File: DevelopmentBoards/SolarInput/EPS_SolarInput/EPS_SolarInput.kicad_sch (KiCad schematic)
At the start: 10 parts, among them J1 2053380004, J2 Conn_01x04_Socket, J3 Conn_01x02_Socket, J4 Conn_01x02_Pin, U1 INA232AIDDFR

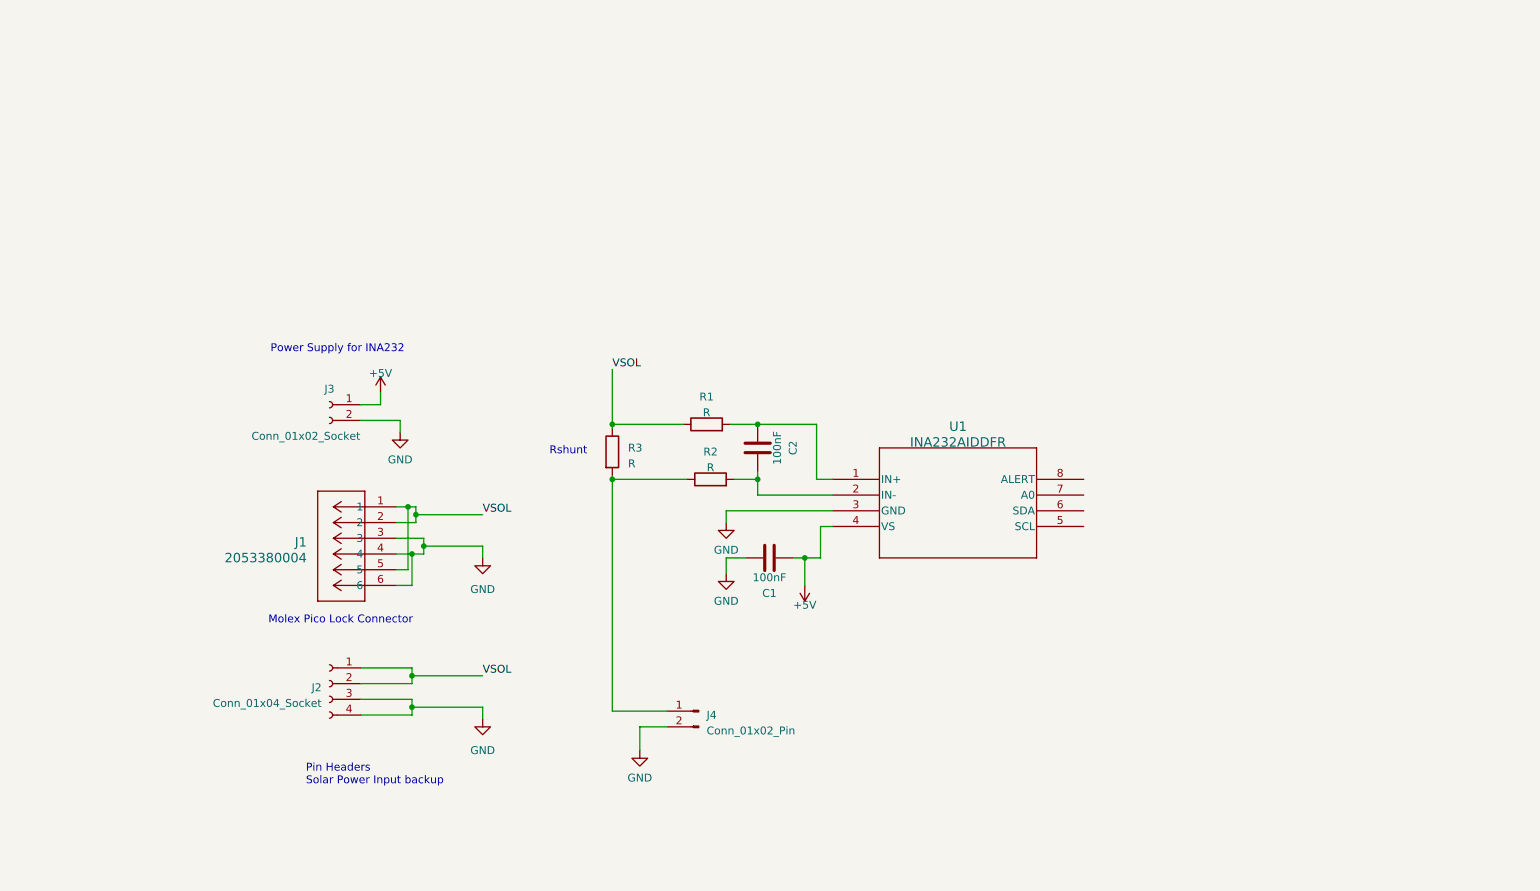
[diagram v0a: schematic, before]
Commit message: Completed EPS Solar Input Schematic
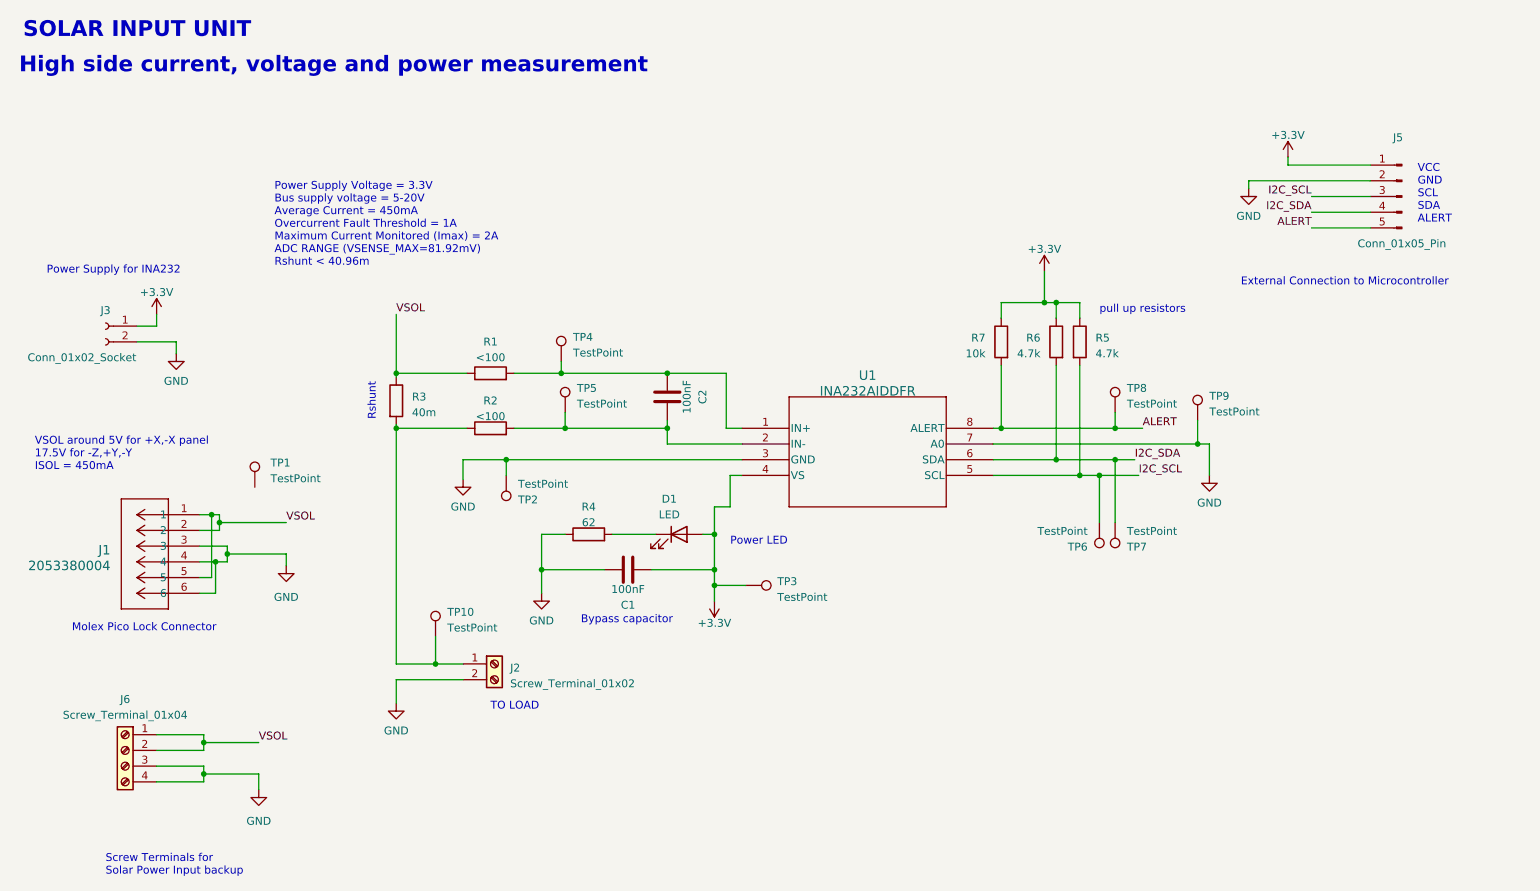
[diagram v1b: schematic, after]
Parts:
- removed J2: Conn_01x04_Socket, symbol Connector:Conn_01x04_Socket
- removed J4: Conn_01x02_Pin, symbol Connector:Conn_01x02_Pin
- added D1: LED, LED_SMD:LED_0805_2012Metric, symbol Device:LED
- added J2: Screw_Terminal_01x02, TerminalBlock_TE-Connectivity:TerminalBlock_TE_282834-2_1x02_P2.54mm_Horizontal, symbol Connector:Screw_Terminal_01x02
- added J5: Conn_01x05_Pin, Connector_PinHeader_2.54mm:PinHeader_1x05_P2.54mm_Vertical, symbol Connector:Conn_01x05_Pin
- added J6: Screw_Terminal_01x04, TerminalBlock_TE-Connectivity:TerminalBlock_TE_282834-4_1x04_P2.54mm_Horizontal, symbol Connector:Screw_Terminal_01x04
- added R4: 62, Resistor_SMD:R_1206_3216Metric, symbol Device:R
- added R5, R6: 4.7k, Resistor_SMD:R_1206_3216Metric, symbol Device:R
- added R7: 10k, Resistor_SMD:R_1206_3216Metric, symbol Device:R
- added TP1, TP10, TP2, TP3, TP4, TP5, TP6, TP7, TP8, TP9: TestPoint, TestPoint:TestPoint_Pad_D2.0mm, symbol Connector:TestPoint
- C1, C2: footprint (none) -> Capacitor_SMD:C_1206_3216Metric
- J1: footprint CON_2053380004 -> Molex-PicoLock_FootprintLib:CON_2053380004
- J3: footprint (none) -> Connector_PinHeader_2.54mm:PinHeader_1x02_P2.54mm_Vertical
- R1, R2: value R -> <100; footprint (none) -> Resistor_SMD:R_1206_3216Metric
- R3: value R -> 40m; footprint (none) -> Resistor_SMD:R_1206_3216Metric
- U1: footprint SOT_32AIDDFR_TEX -> INA232_FootprintLib:SOT_32AIDDFR_TEX
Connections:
- net GND: now also U1.7 (A0), J2.2 (Pin_2), J5.2 (Pin_2), J6.3 (Pin_3), J6.4 (Pin_4), R4.1, TP2.1, TP9.1
- net VSOL: now also J6.1 (Pin_1), J6.2 (Pin_2)
- net at C2.2, R1.2, U1.1 (IN+): now also TP4.1
- net at C2.1, R2.2, U1.2 (IN-): now also TP5.1
- net I2C_SCL: now reaches U1.5 (SCL)
- net I2C_SCL: now also J5.3 (Pin_3), R5.2, TP6.1
- net I2C_SDA: now reaches U1.6 (SDA)
- net I2C_SDA: now also J5.4 (Pin_4), R6.2, TP7.1
- net ALERT: now reaches U1.8 (ALERT)
- net ALERT: now also J5.5 (Pin_5), R7.2, TP8.1
- net at R2.1, R3.2: now also J2.1 (Pin_1), TP10.1
- net +5V renamed +3.3V
- net +3.3V: now also D1.2 (A), J5.1 (Pin_1), R5.1, R6.1, R7.1, TP3.1
- new net: D1.1 (K), R4.2
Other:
- note added: "Bypass capacitor"
- note added: "External Connection to Microcontroller"
- note added: "High side current, voltage and power measurement"
- note added: "Power LED"
- note added: "Power Supply Voltage = 3.3V Bus supply voltage = 5-20V Average Current = 450mA Overcurrent Fault Threshold = 1A Maximum Current Monitored (Imax) = 2A ADC RANGE (VSENSE_MAX=81.92mV) Rshunt < 40.96m"
- note added: "SOLAR INPUT UNIT"
- note added: "Screw Terminals for Solar Power Input backup"
- note added: "TO LOAD"
- note added: "VCC GND SCL SDA ALERT"
- note added: "VSOL around 5V for +X,-X panel 17.5V for -Z,+Y,-Y ISOL = 450mA"
- note added: "pull up resistors"
- note removed: "Pin Headers Solar Power Input backup"
- moved on the sheet: C1, C2, J1, J3, R1, R2, R3, U1

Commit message: Completed PCB Design for Solar Input Unit Development Board
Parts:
- added J4: Conn_01x02_Socket, Connector_PinHeader_2.54mm:PinHeader_1x02_P2.54mm_Vertical, symbol Connector:Conn_01x02_Socket
- added TP10, TP12: TestPoint, TestPoint:TestPoint_Pad_D1.0mm, symbol Connector:TestPoint
- TP1, TP2, TP3, TP4, TP5, TP6, TP7, TP8, TP9: footprint TestPoint:TestPoint_Pad_D2.0mm -> TestPoint:TestPoint_Pad_D1.0mm
- TP11: renamed from TP10; footprint TestPoint:TestPoint_Pad_D2.0mm -> TestPoint:TestPoint_Pad_D1.0mm
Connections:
- net +3.3V: now also TP10.1
- net ALERT: now also J5.3 (Pin_3); no longer J5.5 (Pin_5)
- net GND: now also J1.5, TP12.1
- net I2C_SCL: now also J5.5 (Pin_5); no longer J5.3 (Pin_3)
- net VSOL: now also TP1.1; no longer J1.5
- net at C2.1, R2.2, TP5.1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: now also J4.2 (Pin_2)
- net at C2.2, R1.2, TP4.1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: now also J4.1 (Pin_1)
